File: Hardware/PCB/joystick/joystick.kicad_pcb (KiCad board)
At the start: 2 copper layers, 192 x 107 mm, 62 parts, among them J1 Synth_power_2x5, J2 6 pin Molex header, J3 AudioJack2, J4 AudioJack2, J5 Conn_01x11, J6 AudioJack2, J7 AudioJack2, J8 Conn_01x11, U1 TL074, U2 TL074

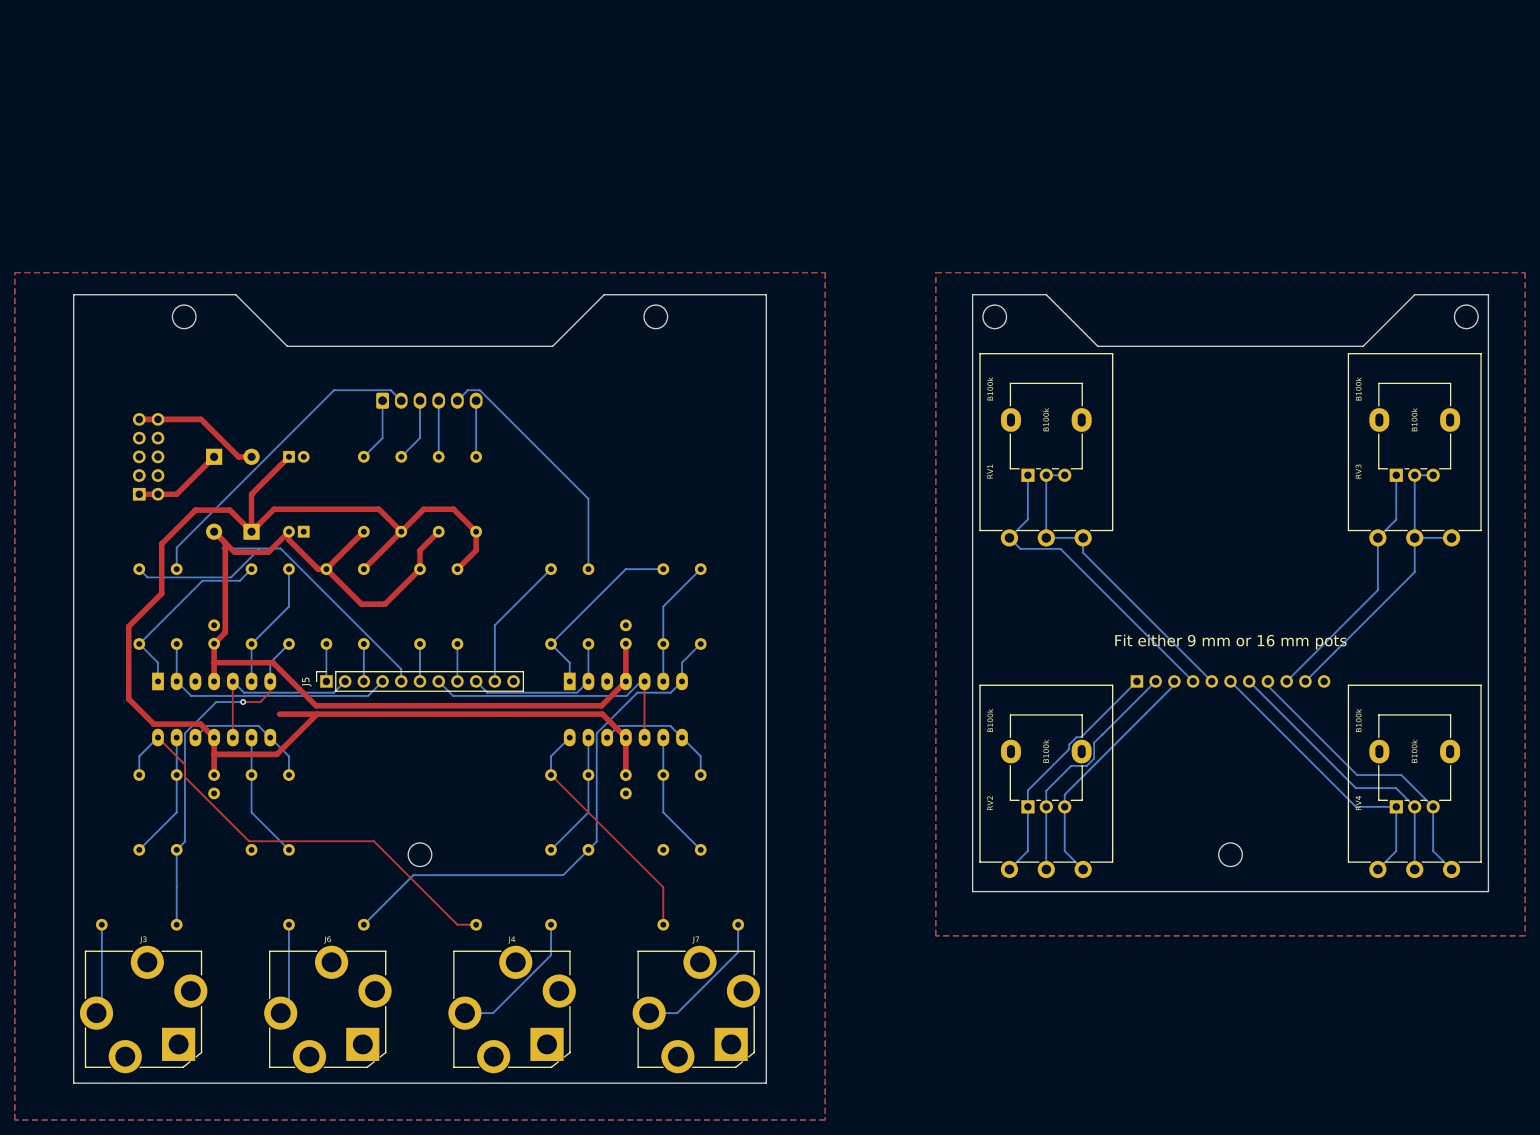
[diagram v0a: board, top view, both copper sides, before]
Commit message: Belated .gitignore; switch to panel mounted pots implying board and panel changes
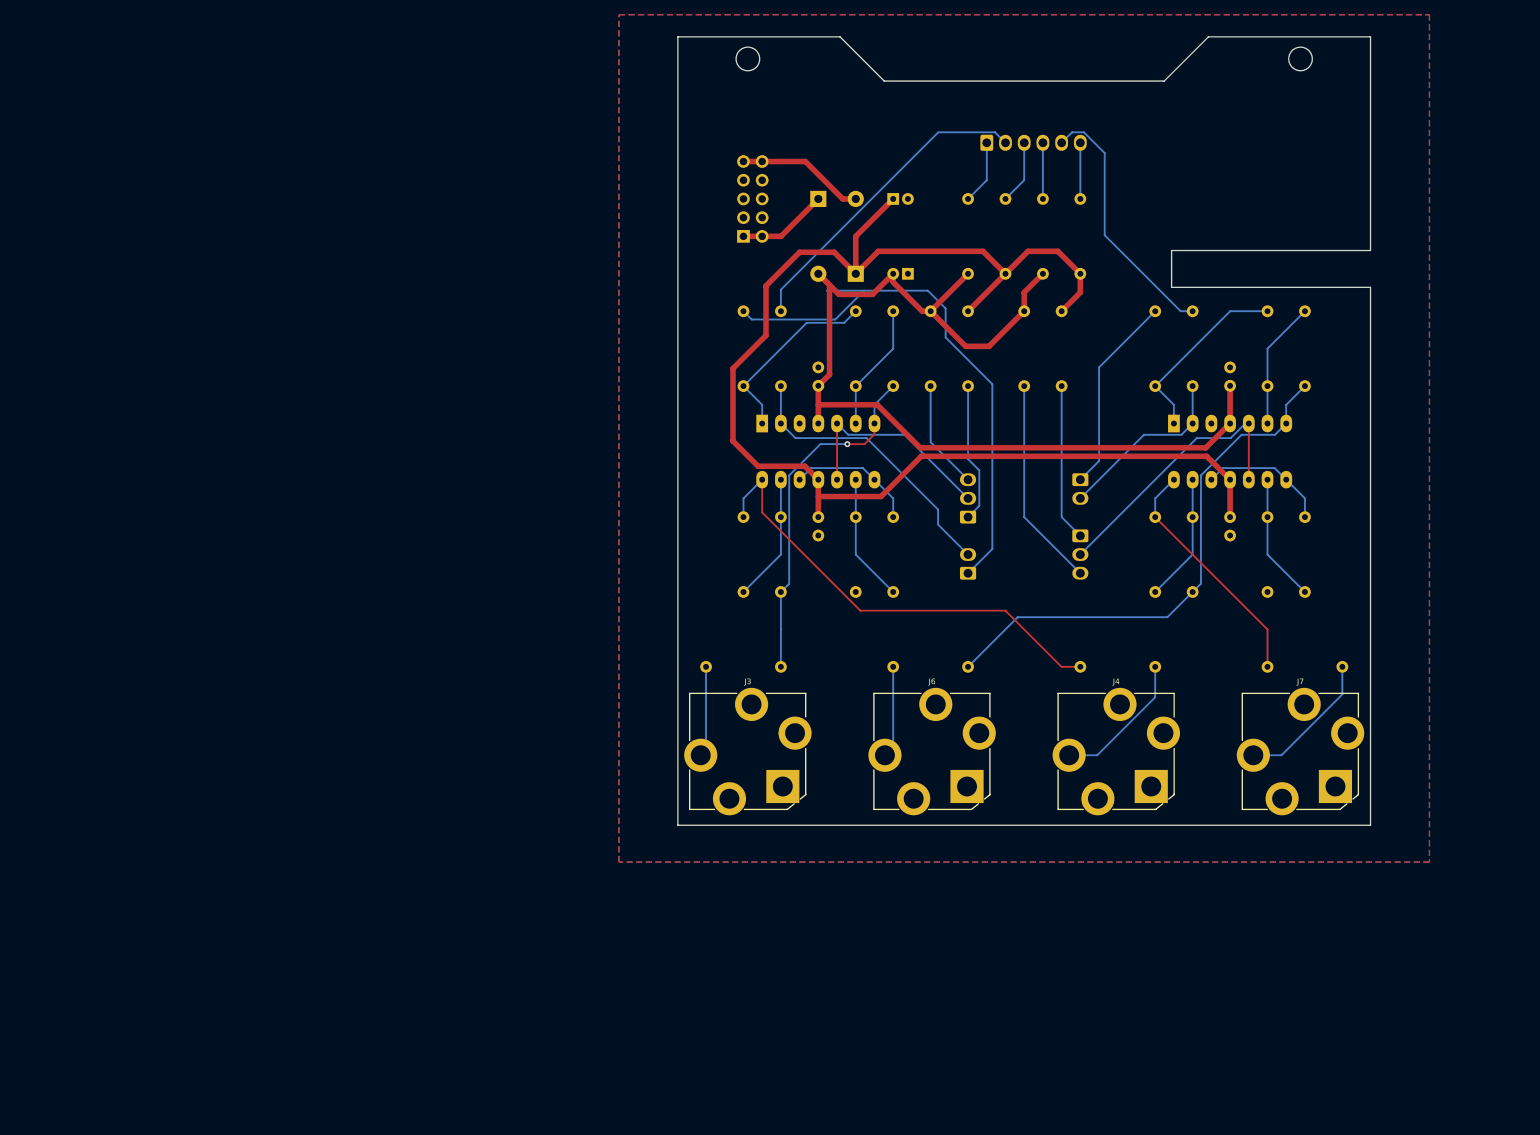
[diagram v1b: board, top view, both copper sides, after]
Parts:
- removed H3, H4, H5, H6: MountingHole, ao_tht:MountingHole_3.2mm_M3
- removed J5: Conn_01x11, Connector_PinSocket_2.54mm:PinSocket_1x11_P2.54mm_Vertical
- removed J8: Conn_01x11, Connector_PinHeader_2.54mm:PinHeader_1x11_P2.54mm_Vertical
- removed RV1, RV2, RV3, RV4: B100k, ao_tht:Potentiometer_Alpha_16mm_Single_Vertical
- removed RV5, RV6, RV7, RV8: B100k, ao_tht:Potentiometer_Alpha_RD901F-40-00D_Single_Vertical_centered
- added GRAF3: CC0 logo, ao_tht:CC0_logo, B.Cu at (175.0, 71.0)
- added J10: 2_pin_Molex_header, ao_tht:Molex_KK-254_AE-6410-02A_1x02_P2.54mm_Vertical, B.Cu at (139.4, 120.8)
- added J13: 3_pin_Molex_header, ao_tht:Molex_KK-254_AE-6410-03A_1x03_P2.54mm_Vertical, B.Cu at (154.6, 115.7)
- added J14: 2_pin_Molex_header, ao_tht:Molex_KK-254_AE-6410-02A_1x02_P2.54mm_Vertical, B.Cu at (154.6, 108.1)
- added J9: 3_pin_Molex_header, ao_tht:Molex_KK-254_AE-6410-03A_1x03_P2.54mm_Vertical, B.Cu at (139.4, 113.2)
- GRAF1: footprint joystick_pcb:joystick_panel_holes -> joystick_panel:joystick_panel_holes
- GRAF2: value Holes -> AO logo; footprint joystick_pcb:joystick_panel_holes -> ao_tht:analogoutput_12mm; moved to B.Cu
- moved H2 94.2 mm to (184.5, 51.0)
- moved R14 89.2 mm to (134.3, 95.4)
- moved R17 89.2 mm to (152.1, 85.2)
- moved R19 89.2 mm to (169.9, 95.4)
- moved R21 89.2 mm to (180.0, 95.4)
- moved R23 89.2 mm to (180.0, 113.2)
- moved R26 89.2 mm to (169.9, 113.2)
- moved C1 89.2 mm to (129.2, 70.0)
- moved C2 89.2 mm to (131.2, 80.2)
- moved C3 89.2 mm to (119.1, 113.2)
- moved C4 89.2 mm to (119.1, 92.9)
- moved C5 89.2 mm to (174.9, 113.2)
- moved C6 89.2 mm to (174.9, 92.9)
- moved D1 89.2 mm to (124.1, 80.2)
- moved D2 89.2 mm to (119.1, 70.0)
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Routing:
- net XRANGEPOT_WIPER_P: track 42.7 -> 0.00 mm
- net XRANGEPOT_CCW_P: track 42.5 -> 0.00 mm
- net YRANGEPOT_WIPER_P: track 41.6 -> 0.00 mm
- net YOFFPOT_CW_P: track 39.4 -> 0.00 mm
- net YOFFPOT_CCW_P: track 39.1 -> 0.00 mm
- net YOFFPOT_WIPER_P: track 38.0 -> 0.00 mm
- net YRANGEPOT_CCW_P: track 34.1 -> 0.00 mm
- net XOFFPOT_CCW_P: track 33.1 -> 0.00 mm
- net XOFFPOT_WIPER_P: track 32.9 -> 0.00 mm
- net XOFFPOT_CW_P: track 32.7 -> 0.00 mm
- net XRANGEPOT_WIPER: track 51.2 -> 75.5 mm
- net YOFFPOT_CCW: track 5.08 -> 28.6 mm
- net YOFFPOT_CW: track 5.08 -> 21.4 mm
- net XOFFPOT_CW: track 5.08 -> 19.0 mm
- net XOFFPOT_CCW: track 5.08 -> 14.8 mm
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- removed copper zone on B.Cu, net GND1
- removed copper zone on F.Cu, net GND1
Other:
- board size 192 x 107 mm -> 94 x 107 mm
- board text added: "JOYSTICK"
- board text added: "Joystick"
- board text added: "Rich Holmes CC0 1.0 / October 2021 https://github.com/holmesrichards/joystick"
- board text added: "X ccw"
- board text added: "X cw"
- board text added: "X offset ccw/w/cw"
- board text added: "X range ccw/w"
- board text added: "X w"
- board text added: "Y ccw"
- board text added: "Y cw"
- board text added: "Y offset cw/w/ccw"
- board text added: "Y range w/ccw"
- board text added: "Y w"
- board text removed: "Fit either 9 mm or 16 mm pots"

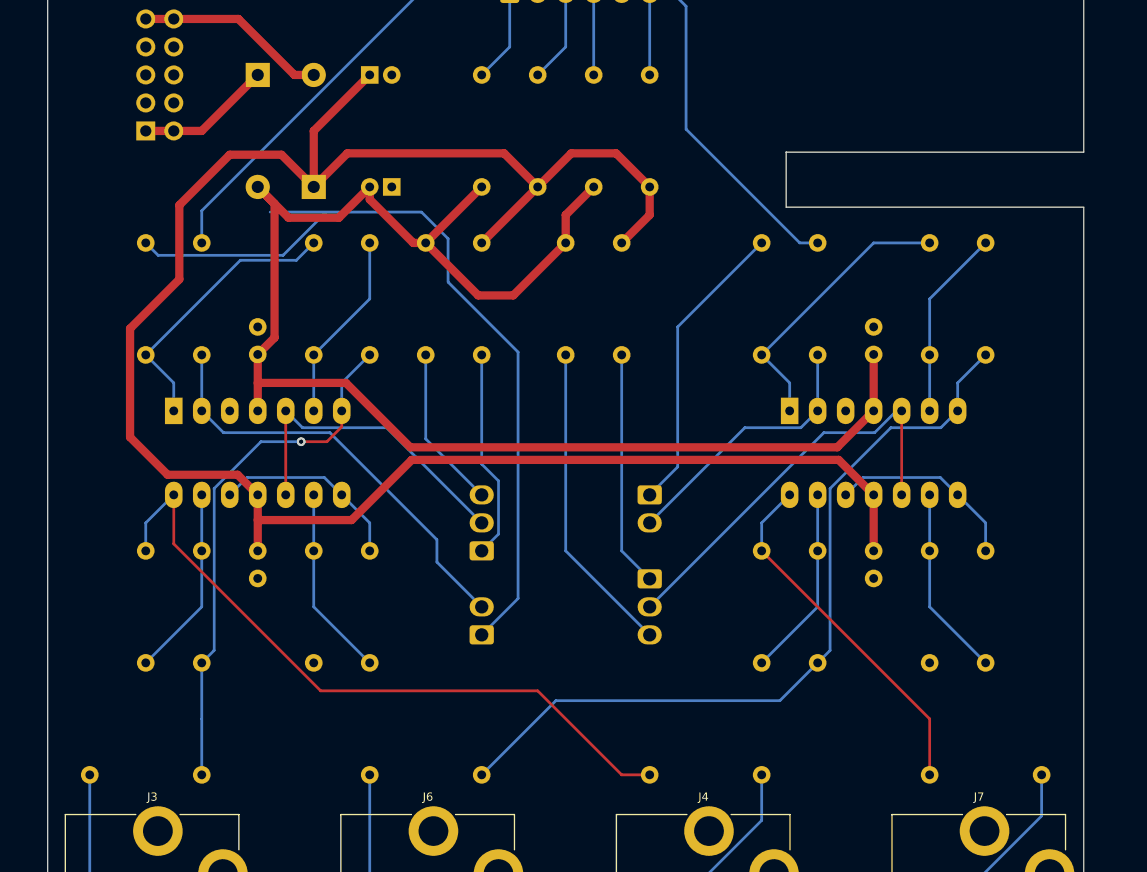
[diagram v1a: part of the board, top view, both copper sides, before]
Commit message: Add gain trimmers and test points
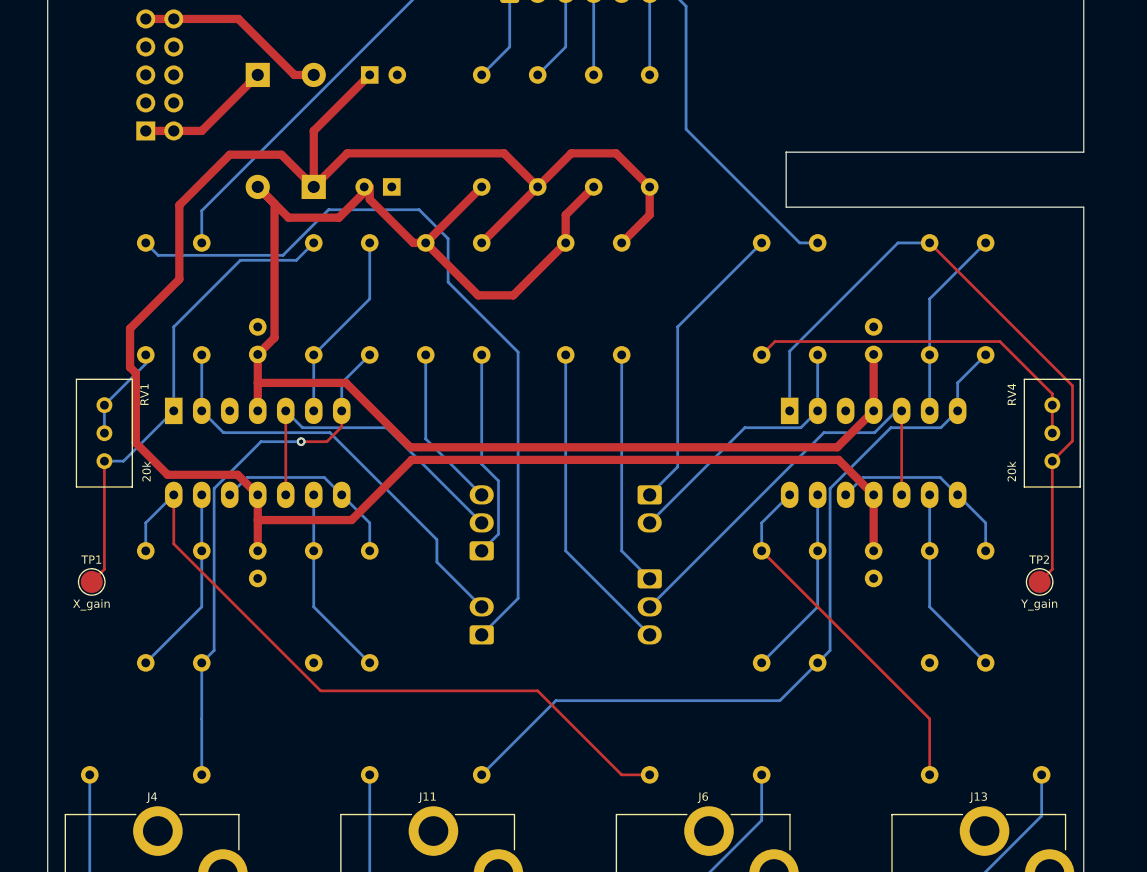
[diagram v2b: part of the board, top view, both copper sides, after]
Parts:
- added RV1: 20k, ao_tht:Potentiometer_Bourns_3296W_Vertical_screw_centered, F.Cu at (104.0, 106.0)
- added RV4: 20k, ao_tht:Potentiometer_Bourns_3296W_Vertical_screw_centered, F.Cu at (190.0, 106.0)
- added TP1: X_gain, TestPoint:TestPoint_Pad_D2.0mm, F.Cu at (104.0, 116.0)
- added TP2: Y_gain, TestPoint:TestPoint_Pad_D2.0mm, F.Cu at (190.0, 116.0)
- C1, C2: footprint ao_tht:CP_Radial_D5.0mm_P2.00mm -> ao_tht:CP_Radial_D6.3mm_P2.50mm
- R2: renamed from R12; value 20k -> 15k
- R20: value 20k -> 10k
- R6: renamed from R2; value 20k -> 10k
- renumbered J6 to J11, J13 to J12, J7 to J13, J3 to J4, J2 to J5, J4 to J6, J9 to J7, J10 to J8, R4 to R1, R7 to R10, R8 to R11, R9 to R12, R10 to R13, R11 to R14, R13 to R3, R14 to R4, R1 to R5, R3 to R7, R5 to R8, R6 to R9
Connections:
- R21 pad 2: Net-(R20-Pad1) -> Net-(R21-Pad2)
- R6 pad 1: Net-(R2-Pad1) -> Net-(R6-Pad1)
- R7 pad 2: Net-(R2-Pad1) -> Net-(R7-Pad2)
- U1 pad 1: Net-(R2-Pad1) -> Net-(R7-Pad2)
- U2 pad 1: Net-(R20-Pad1) -> Net-(R21-Pad2)
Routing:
- net Net-(R21-Pad2): track 0.00 -> 59.5 mm
- net Net-(R7-Pad2): track 0.00 -> 43.1 mm
- net Net-(R2-Pad1): track 25.6 -> 0.00 mm
- net Net-(R6-Pad1): track 0.00 -> 8.65 mm
- net Net-(R20-Pad1): track 25.6 -> 32.4 mm
- net XRANGEPOT_WIPER: track 75.5 -> 70.6 mm

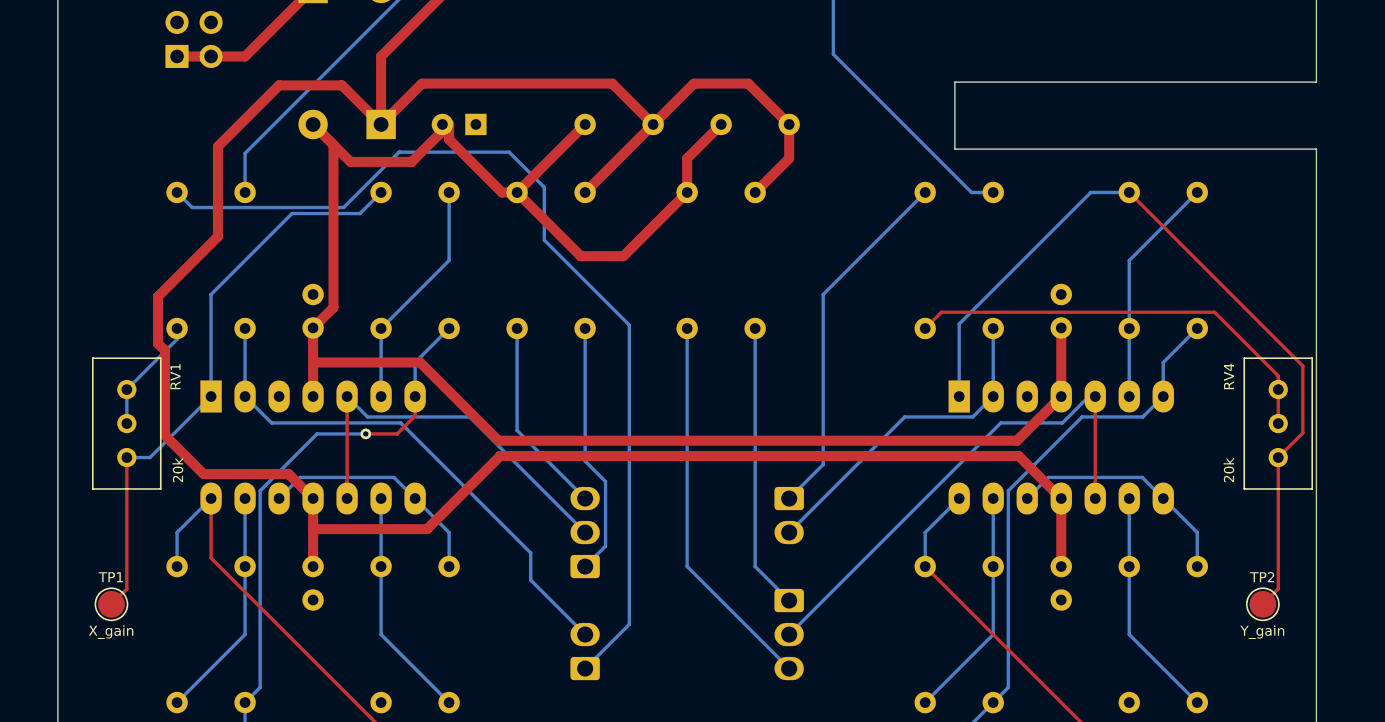
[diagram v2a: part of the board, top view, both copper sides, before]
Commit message: Move trimmers to inputs
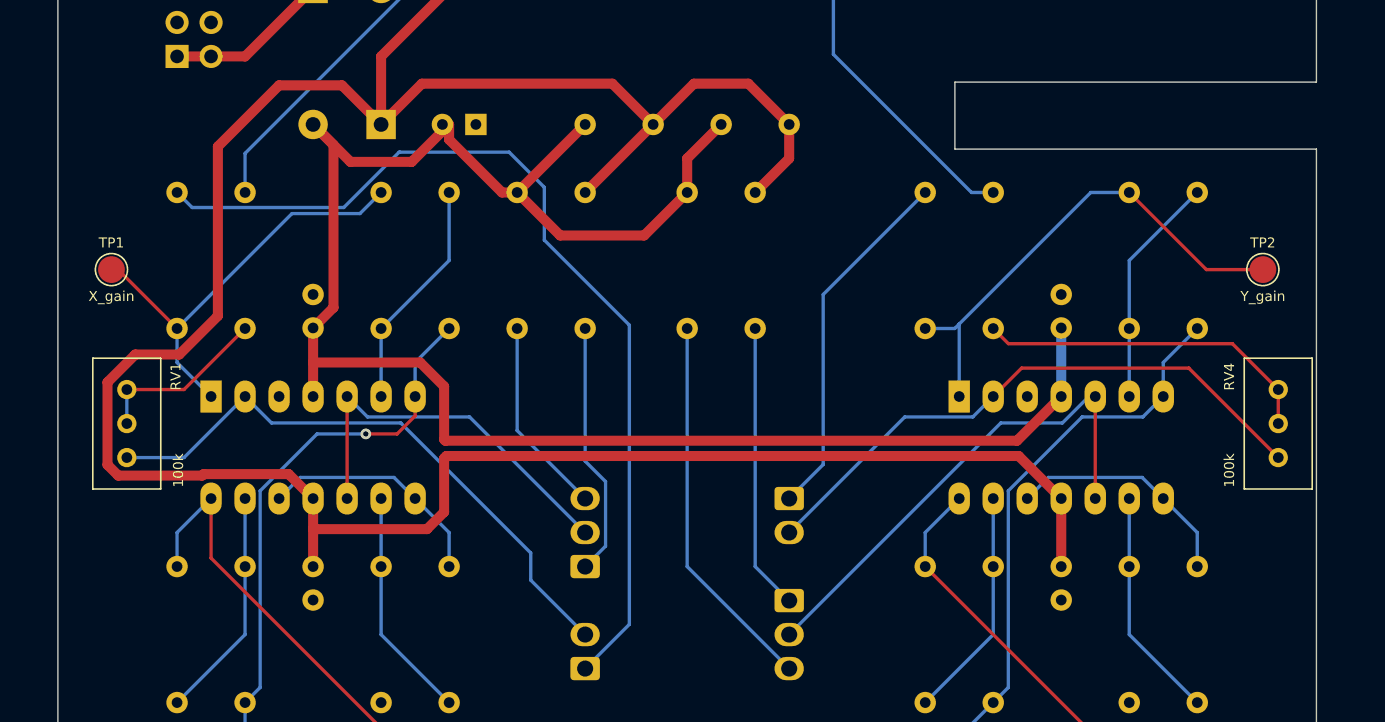
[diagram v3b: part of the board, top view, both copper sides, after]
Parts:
- R17: renamed from R19; value 120k -> 68k
- R20, R6: value 10k -> 20k
- R3: renamed from R5; value 120k -> 68k
- RV1, RV4: value 20k -> 100k
- moved TP1 25.0 mm to (104.0, 91.0)
- moved TP2 25.0 mm to (190.0, 91.0)
- renumbered R17 to R18, R18 to R19, R3 to R4, R4 to R5
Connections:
- R17 pad 1: YRANGEPOT_CCW -> Net-(R17-Pad1)
- R21 pad 2: Net-(R21-Pad2) -> Net-(R20-Pad1)
- R3 pad 1: XRANGEPOT_CCW -> Net-(R3-Pad1)
- R7 pad 2: Net-(R7-Pad2) -> Net-(R6-Pad1)
- RV1 pad 1: Net-(R7-Pad2) -> XRANGEPOT_CCW
- RV1 pad 2: Net-(R6-Pad1) -> Net-(R3-Pad1)
- RV1 pad 3: Net-(R6-Pad1) -> Net-(R3-Pad1)
- RV4 pad 1: Net-(R21-Pad2) -> YRANGEPOT_CCW
- RV4 pad 2: Net-(R20-Pad1) -> Net-(R17-Pad1)
- RV4 pad 3: Net-(R20-Pad1) -> Net-(R17-Pad1)
- TP1 pad 1: Net-(R7-Pad2) -> Net-(R6-Pad1)
- TP2 pad 1: Net-(R21-Pad2) -> Net-(R20-Pad1)
- U1 pad 1: Net-(R7-Pad2) -> Net-(R6-Pad1)
- U2 pad 1: Net-(R21-Pad2) -> Net-(R20-Pad1)
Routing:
- net Net-(R21-Pad2): track 59.5 -> 0.00 mm
- net Net-(R7-Pad2): track 43.1 -> 0.00 mm
- net Net-(R17-Pad1): track 0.00 -> 25.7 mm
- net Net-(R6-Pad1): track 8.65 -> 32.3 mm
- net YRANGEPOT_CCW: track 24.5 -> 44.4 mm
- net Net-(R3-Pad1): track 0.00 -> 13.3 mm
- net +12V: track 182.7 -> 194.0 mm
- net XRANGEPOT_CCW: track 39.0 -> 44.7 mm
- net Net-(R20-Pad1): track 32.4 -> 37.2 mm
- net -12V: track 136.7 -> 137.7 mm

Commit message: More tweaks, build.md
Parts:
- moved GRAF1 24.2 mm to (157.0, 92.0)
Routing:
- net +12V: track 194.0 -> 182.6 mm
